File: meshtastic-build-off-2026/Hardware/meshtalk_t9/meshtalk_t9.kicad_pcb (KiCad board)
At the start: 4 copper layers, 45.8 x 79.2 mm, 44 parts, among them J1 USB_C_Receptacle_USB2.0_16P, J2 Conn_01x02_Socket, Q1 Q_PMOS_GSD, SW1 SW_Push, SW10 SW_Push, SW11 SW_Push, SW12 SW_Push, SW13 SW_Push, SW14 SW_Push, SW15 SW_Push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

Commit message: rename + battery % + boot btn changed to reset + fix battery chrging
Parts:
- added Q2: 2N7002, Package_TO_SOT_SMD:SOT-23, F.Cu at (43.8, 66.0)
- added R5: 390k, Capacitor_SMD:C_0805_2012Metric, F.Cu at (46.8, 68.0)
- added R6: 100k, Capacitor_SMD:C_0805_2012Metric, F.Cu at (46.8, 71.8)
- added R7: 2k, Capacitor_SMD:C_0805_2012Metric, F.Cu at (48.8, 46.5)
- moved C6 22.4 mm to (40.0, 63.2)
- moved Q1 2.85 mm to (49.6, 42.2), turned to 180 degrees
- moved SW1 1.75 mm to (54.0, 69.2)
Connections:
- Q1 pad 2: Net-(J2-Pin_1) -> /Power_Management/V_SYS
- Q1 pad 3: /Power_Management/V_SYS -> Net-(J2-Pin_1)
- SW1 pad 2: Net-(U1-IO0) -> Net-(U1-EN)
- U1 pad 15: unconnected-(U1-IO3-Pad15) -> /MCU_Core/BATTERY_PIN
- U1 pad 24: unconnected-(U1-IO47-Pad24) -> /MCU_Core/ADC_CTRL
- U1 pad 27: Net-(U1-IO0) -> unconnected-(U1-IO0-Pad27)
- U3 pad 8: unconnected-(U3-PROG-Pad8) -> Net-(U3-PROG)
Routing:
- net /MCU_Core/BATTERY_PIN: track 0.00 -> 49.3 mm, vias 0 -> 4
- net Net-(U1-EN): track 14.9 -> 60.3 mm, vias 0 -> 2
- net /MCU_Core/ADC_CTRL: track 0.00 -> 19.0 mm
- net Net-(U1-IO0): track 16.2 -> 0.00 mm
- net Net-(J2-Pin_1): track 32.6 -> 40.2 mm
- net Net-(Q2-D): track 0.00 -> 7.16 mm
- net Net-(U3-PROG): track 0.00 -> 2.75 mm
- net GND: track 40.8 -> 42.9 mm, vias 12 -> 14
- net +3V3: track 91.3 -> 93.0 mm, vias 6 -> 5
- net Net-(D1-A): track 33.8 -> 32.4 mm
- net /Power_Management/V_SYS: track 41.2 -> 40.0 mm

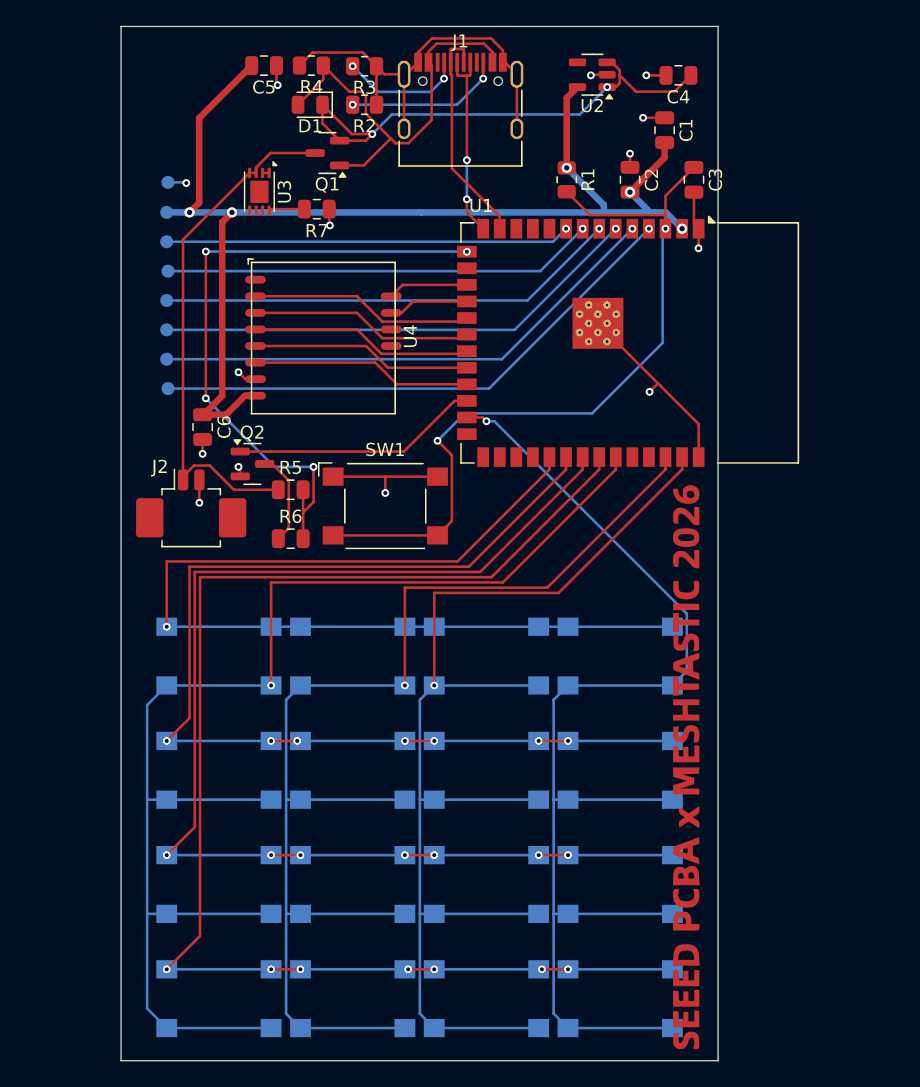
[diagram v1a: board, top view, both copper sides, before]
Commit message: Replace AP2112K-3.3  with AP7361C-33E Connected LORA RF_SW1 to GPIO Added ESD Added mounting holes for display (Waveshare 2 inch) Added Boot and Reset buttons made power rails thicker added dedicated layer for 3v3 and GND
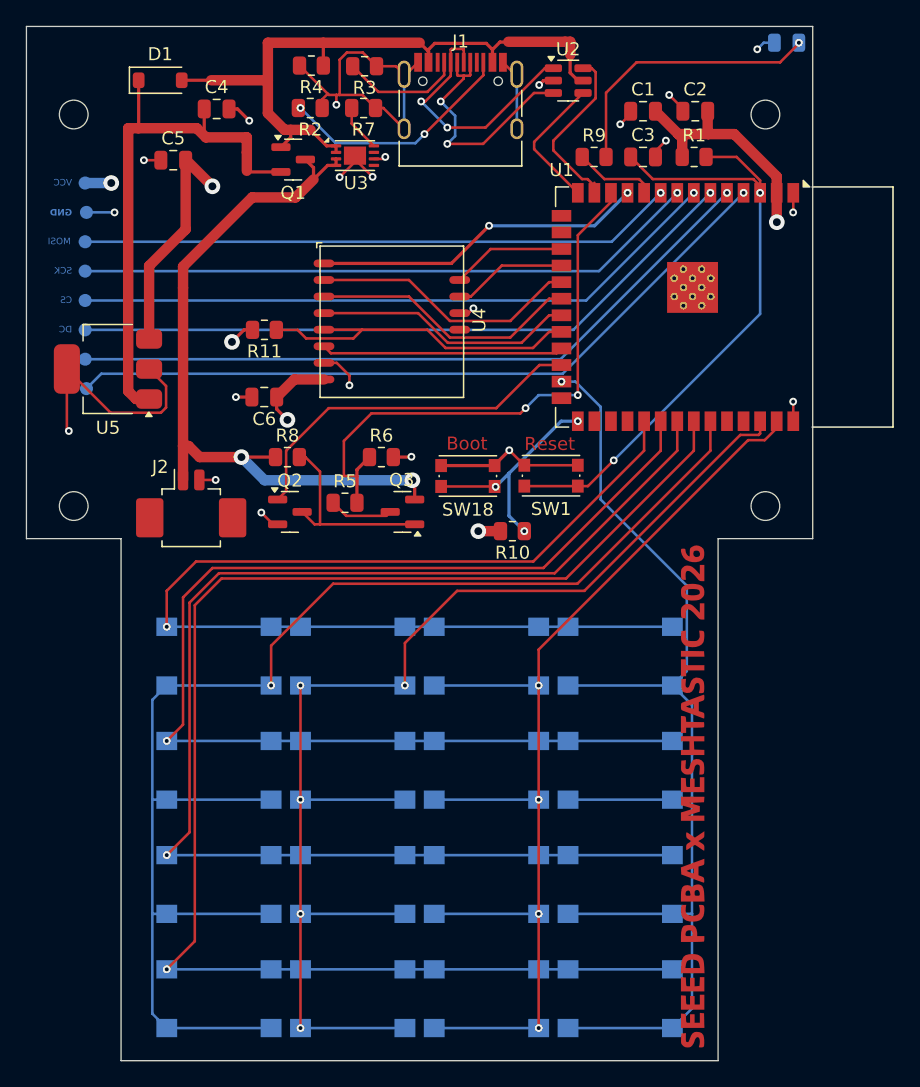
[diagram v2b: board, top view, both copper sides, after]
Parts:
- added D2: LED, LED_SMD:LED_0805_2012Metric, B.Cu at (84.8, 33.8)
- added H1: MountingHole, MountingHole:MountingHole_2.2mm_M2, F.Cu at (83.1, 69.2)
- added H2: MountingHole, MountingHole:MountingHole_2.2mm_M2, F.Cu at (83.1, 39.2)
- added H3: MountingHole, MountingHole:MountingHole_2.2mm_M2, F.Cu at (30.1, 39.2)
- added H4: MountingHole, MountingHole:MountingHole_2.2mm_M2, F.Cu at (30.1, 69.2)
- added Q3: Q_PMOS_GSD, Package_TO_SOT_SMD:SOT-23, F.Cu at (55.3, 69.7)
- added R10: 10k, Resistor_SMD:R_0805_2012Metric, F.Cu at (63.7, 71.2)
- added R11: 10k, Resistor_SMD:R_0805_2012Metric, F.Cu at (44.7, 55.8)
- added R8: 100k, Resistor_SMD:R_0805_2012Metric, F.Cu at (46.5, 65.5)
- added R9: 470, Resistor_SMD:R_0805_2012Metric, F.Cu at (70.0, 42.5)
- added SW18: SW_Push, Button_Switch_SMD:SW_Push_1P1T_NO_CK_KMR2, F.Cu at (60.3, 67.0)
- added U5: AP7361C-33E, Package_TO_SOT_SMD:SOT-223-3_TabPin2, F.Cu at (32.8, 58.8)
- C1, C4, C5: value 10uF -> 10uF 16V X5R
- C3: value 0.1uf -> 0.1uF
- D1: footprint LED_SMD:LED_0805_2012Metric -> Diode_SMD:D_SOD-123
- R5, R6, R7: footprint Capacitor_SMD:C_0805_2012Metric -> Resistor_SMD:R_0805_2012Metric
- SW1: footprint Button_Switch_SMD:SW_SPST_Omron_B3FS-100xP -> Button_Switch_SMD:SW_Push_1P1T_NO_CK_KMR2
- U2: value AP2112K-3.3 -> USBLC6-2SC6; footprint Package_TO_SOT_SMD:SOT-23-5 -> Package_TO_SOT_SMD:SOT-23-6
- moved C4 35.5 mm to (41.1, 38.8), turned to 0 degrees
- moved SW1 12.9 mm to (66.7, 66.9)
- moved D1 11.7 mm to (36.8, 36.6), turned to 0 degrees
- moved C5 10.1 mm to (37.8, 42.8), turned to 0 degrees
- moved R1 9.92 mm to (77.7, 42.5), turned to 0 degrees
- moved R6 9.35 mm to (53.7, 65.5)
- moved R7 8.54 mm to (52.3, 38.8)
- moved U3 7.83 mm to (51.7, 42.4), turned to 0 degrees
- moved U1 7.75 mm to (80.0, 54.0)
- moved TP2 7.70 mm to (31.0, 53.5)
- moved TP4 7.70 mm to (31.0, 58.0)
- moved C2 7.25 mm to (77.8, 39.0), turned to 0 degrees
- moved TP5 6.74 mm to (31.0, 49.0)
- moved TP8 6.66 mm to (31.1, 46.8)
- moved TP6 6.64 mm to (31.0, 51.2)
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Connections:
- net /LoRa_Radio/LORA_DI02 renamed /LoRa_Radio/LORA_BUSY
- J1 pad A1: Net-(J1-SHIELD) -> GND
- J1 pad A12: Net-(J1-SHIELD) -> GND
- J1 pad A6: /MCU_Core/USB_D+ -> Net-(J1-D+-PadA6)
- J1 pad A7: /MCU_Core/USB_D- -> Net-(J1-D--PadA7)
- J1 pad B1: Net-(J1-SHIELD) -> GND
- J1 pad B12: Net-(J1-SHIELD) -> GND
- J1 pad B6: /MCU_Core/USB_D+ -> Net-(J1-D+-PadA6)
- J1 pad B7: /MCU_Core/USB_D- -> Net-(J1-D--PadA7)
- J1 pad S1: Net-(J1-SHIELD) -> GND
- R2 pad 1: Net-(J1-SHIELD) -> GND
- R3 pad 1: Net-(J1-SHIELD) -> GND
- R4 pad 2: Net-(J1-SHIELD) -> GND
- R5 pad 1: Net-(J2-Pin_1) -> Net-(Q3-D)
- R6 pad 1: Net-(Q2-D) -> /MCU_Core/BATTERY_PIN
- R6 pad 2: /MCU_Core/BATTERY_PIN -> GND
- U1 pad 10: unconnected-(U1-IO17-Pad10) -> Net-(U1-IO17)
- U1 pad 11: unconnected-(U1-IO18-Pad11) -> /LoRa_Radio/LORA_RF_SW1
- U1 pad 12: unconnected-(U1-IO8-Pad12) -> /MCU_Core/BATTERY_PIN
- U1 pad 15: /MCU_Core/BATTERY_PIN -> unconnected-(U1-IO3-Pad15)
- U1 pad 27: unconnected-(U1-IO0-Pad27) -> Net-(U1-IO0)
- U1 pad 5: /MCU_Core/DISPLAY_CS -> /MCU_Core/TFT_RST
- U1 pad 7: /MCU_Core/TFT_RST -> /MCU_Core/DISPLAY_CS
- U1 pad 8: /MCU_Core/TFT_MOSI -> /MCU_Core/TFT_SCK
- U1 pad 9: /MCU_Core/TFT_SCK -> /MCU_Core/TFT_MOSI
- U2 pad 1: /Power_Management/V_SYS -> Net-(J1-D--PadA7)
- U2 pad 3: /Power_Management/V_SYS -> Net-(J1-D+-PadA6)
- U2 pad 4: unconnected-(U2-NC-Pad4) -> /MCU_Core/USB_D+
- U2 pad 5: +3V3 -> Net-(D1-A)
- U3 pad 1: Net-(U3-V_{DD}-Pad1) -> Net-(D1-A)
- U3 pad 2: Net-(U3-V_{DD}-Pad1) -> Net-(D1-A)
- U3 pad 6: unconnected-(U3-V_{SS}-Pad6) -> GND
- U3 pad 9: (no net) -> GND
- U4 pad 1: unconnected-(U4-RF_SW1-Pad1) -> /LoRa_Radio/LORA_RF_SW1
- U4 pad 10: unconnected-(U4-GND2-Pad10) -> GND
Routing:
- net GND: track 42.9 -> 91.6 mm, vias 14 -> 22
- net +3V3: track 93.0 -> 48.6 mm, vias 5 -> 6
- net Net-(J1-SHIELD): track 32.3 -> 0.00 mm
- net /LoRa_Radio/LORA_RF_SW1: track 0.00 -> 25.5 mm, vias 0 -> 2
- net Net-(D2-A): track 0.00 -> 21.4 mm, vias 0 -> 1
- net Net-(D1-A): track 32.4 -> 52.6 mm
- net Net-(J1-D--PadA7): track 0.00 -> 19.9 mm, vias 0 -> 2
- net Net-(J1-D+-PadA6): track 0.00 -> 19.4 mm, vias 0 -> 2
- net /MCU_Core/TFT_RST: track 35.4 -> 54.5 mm
- net Net-(U1-IO0): track 0.00 -> 17.5 mm, vias 0 -> 3
- net /MCU_Core/TFT_SCK: track 31.0 -> 47.9 mm
- net Net-(J2-Pin_1): track 40.2 -> 56.5 mm, vias 0 -> 2
- net /MCU_Core/TFT_DC: track 37.6 -> 52.3 mm
- net /MCU_Core/TFT_BL: track 41.9 -> 56.6 mm
- net /MCU_Core/TFT_MOSI: track 33.1 -> 45.7 mm
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- added copper zone on In2.Cu, net +3V3
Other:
- board size 45.8 x 79.2 mm -> 60.2 x 79.2 mm
- board text added: "BL"
- board text added: "Boot"
- board text added: "CS"
- board text added: "DC"
- board text added: "GND"
- board text added: "MOSI"
- board text added: "RST"
- board text added: "Reset"
- board text added: "SCK"
- board text added: "VCC"

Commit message: PCB Updates - Align net names Clearence for esp32 antenna
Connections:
- net /MCU_Core/DISPLAY_CS renamed /MCU_Core/TFT_CS
- net /MCU_Core/TFT_SCK renamed /MCU_Core/TFT_CLK
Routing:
- net GND: track 91.6 -> 129.0 mm, vias 22 -> 21
- net +3V3: track 48.6 -> 70.8 mm
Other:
- board text added: "CLK"
- board text removed: "SCK"
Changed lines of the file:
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@@
 	(net 34 "/MCU_Core/TFT_RST")
 	(net 35 "Net-(Q2-D)")
-	(net 36 "/MCU_Core/DISPLAY_CS")
+	(net 36 "/MCU_Core/TFT_CS")
 	(net 37 "/MCU_Core/TFT_BL")
 	(net 38 "unconnected-(U3-STAT-Pad5)")
@@
 	(net 40 "unconnected-(U4-ANT-Pad9)")
 	(net 41 "/MCU_Core/TFT_MOSI")
-	(net 42 "/MCU_Core/TFT_SCK")
+	(net 42 "/MCU_Core/TFT_CLK")
 	(net 43 "/LoRa_Radio/SPI_MOSI_LORA")
 	(net 44 "/LoRa_Radio/SPI_MISO_LORA")
@@
 			)
 		)
-		(property "MPN" "ESP32-S3-WROOM-1-N16R16VA"
+		(property "MPN" "ESP32-S3-WROOM-1-N16R8"
 			(at 0 0 270)
 			(unlocked yes)
@@
 			(size 1.5 0.9)
 			(layers "F.Cu" "F.Mask" "F.Paste")
-			(net 36 "/MCU_Core/DISPLAY_CS")
+			(net 36 "/MCU_Core/TFT_CS")
 			(pinfunction "IO7")
 			(pintype "bidirectional")
@@
 			(size 1.5 0.9)
 			(layers "F.Cu" "F.Mask" "F.Paste")
-			(net 42 "/MCU_Core/TFT_SCK")
+			(net 42 "/MCU_Core/TFT_CLK")
 			(pinfunction "IO15")
 			(pintype "bidirectional")
@@
 			(size 1 1)
 			(layers "B.Cu" "B.Mask")
-			(net 36 "/MCU_Core/DISPLAY_CS")
+			(net 36 "/MCU_Core/TFT_CS")
 			(pinfunction "1")
 			(pintype "passive")
@@
 			(size 1 1)
 			(layers "B.Cu" "B.Mask")
-			(net 42 "/MCU_Core/TFT_SCK")
+			(net 42 "/MCU_Core/TFT_CLK")
 			(pinfunction "1")
 			(pintype "passive")
@@
 		)
 	)
-	(gr_text "SCK"
+	(gr_text "CLK"
 		(at 30 51.5 0)
 		(layer "B.Cu")
@@
 	)
 	(segment
+		(start 83.99 45.25)
+		(end 83.99 55.81)
+		(width 0.8)
+		(layer "F.Cu")
+		(net 1)
+	)
+	(segment
 		(start 38.75 42.75)
 		(end 40.75 44.75)
@@
 	)
 	(segment
-		(start 83.99 47.49)
-		(end 84 47.5)
-		(width 0.8)
-		(layer "F.Cu")
-		(net 1)
-	)
-	(segment
 		(start 45.675 61.825)
 		(end 46.5 62.65)
@@
 	)
 	(segment
-		(start 78.7 39)
-		(end 78.7 40.7)
+		(start 83.99 55.81)
+		(end 81.425 58.375)
 		(width 0.8)
 		(layer "F.Cu")
@@
 	)
 	(segment
-		(start 83.99 45.25)
-		(end 83.99 47.49)
+		(start 78.7 39)
+		(end 78.7 40.7)
 		(width 0.8)
 		(layer "F.Cu")
@@
 	)
 	(segment
+		(start 81.425 58.375)
+		(end 81.075 58.725)
+		(width 0.8)
+		(layer "F.Cu")
+		(net 1)
+	)
+	(segment
 		(start 83.99 44)
 		(end 80.74 40.75)
@@
 	)
 	(segment
+		(start 81.075 58.725)
+		(end 71.325 58.725)
+		(width 0.8)
+		(layer "F.Cu")
+		(net 1)
+	)
+	(segment
 		(start 83.99 44)
 		(end 83.99 45.25)
@@
 	)
 	(via
-		(at 84 47.5)
+		(at 33 44.5)
 		(size 1.2)
 		(drill 0.6)
@@
 	)
 	(via
-		(at 33 44.5)
+		(at 40.75 44.75)
 		(size 1.2)
 		(drill 0.6)
@@
 	)
 	(via
-		(at 40.75 44.75)
+		(at 42.25 56.675)
 		(size 1.2)
 		(drill 0.6)
@@
 	)
 	(via
-		(at 42.25 56.675)
+		(at 71.325 58.725)
 		(size 1.2)
 		(drill 0.6)
@@
 	)
 	(segment
-		(start 74.7 42.05)
-		(end 75.5 41.25)
+		(start 84.01 60.55)
+		(end 71.2 60.55)
 		(width 0.2)
 		(layer "F.Cu")
@@
 	)
 	(segment
-		(start 85.26 46.74)
-		(end 85.25 46.75)
+		(start 74.7 42.05)
+		(end 75.5 41.25)
 		(width 0.2)
 		(layer "F.Cu")
@@
 	)
 	(segment
+		(start 85.26 62.75)
+		(end 85.26 61.8)
+		(width 0.2)
+		(layer "F.Cu")
+		(net 2)
+	)
+	(segment
 		(start 51.675 42.4)
 		(end 51.675 42.875)
@@
 	)
 	(segment
+		(start 85.26 45.25)
+		(end 85.26 59.3)
+		(width 0.2)
+		(layer "F.Cu")
+		(net 2)
+	)
+	(segment
 		(start 66.875 36.65)
 		(end 66.126314 36.65)
@@
 	)
 	(segment
-		(start 85.26 61.26)
-		(end 85.25 61.25)
-		(width 0.2)
-		(layer "F.Cu")
-		(net 2)
-	)
-	(segment
 		(start 49.674 37.749)
 		(end 50.25 37.749)
@@
 	)
 	(segment
-		(start 85.26 62.75)
-		(end 85.26 61.26)
-		(width 0.2)
-		(layer "F.Cu")
-		(net 2)
-	)
-	(segment
 		(start 51.25 59.25)
 		(end 51.25 60)
@@
 	)
 	(segment
+		(start 85.26 61.8)
+		(end 84.01 60.55)
+		(width 0.2)
+		(layer "F.Cu")
+		(net 2)
+	)
+	(segment
 		(start 76.8 38.8)
 		(end 75.75 37.75)
@@
 	)
 	(segment
-		(start 85.26 45.25)
-		(end 85.26 46.74)
-		(width 0.2)
-		(layer "F.Cu")
-		(net 2)
-	)
-	(segment
 		(start 42.675 38.825)
 		(end 43.575 39.725)
@@
 	)
 	(segment
+		(start 85.26 59.3)
+		(end 84.01 60.55)
+		(width 0.2)
+		(layer "F.Cu")
+		(net 2)
+	)
+	(segment
 		(start 62.375 66.15)
 		(end 62.375 66.1)
@@
 	)
 	(via
-		(at 85.25 61.25)
-		(size 0.6)
-		(drill 0.3)
-		(layers "F.Cu" "B.Cu")
-		(net 2)
-	)
-	(via
 		(at 56 65.475)
 		(size 0.6)
@@
 	)
 	(via
-		(at 82.5 34.25)
+		(at 33.25 46.75)
 		(size 0.6)
 		(drill 0.3)
@@
 	)
 	(via
-		(at 33.25 46.75)
+		(at 35.5 42.75)
 		(size 0.6)
 		(drill 0.3)
@@
 	)
 	(via
-		(at 35.5 42.75)
+		(at 65.788157 36.988157)
 		(size 0.6)
 		(drill 0.3)
@@
 	)
 	(via
-		(at 65.788157 36.988157)
+		(at 73.225 33.75)
 		(size 0.6)
 		(drill 0.3)
@@
 	)
 	(via
-		(at 85.25 46.75)
+		(at 71.2 60.55)
 		(size 0.6)
 		(drill 0.3)
@@
 	)
 	(segment
-		(start 83 33.75)
-		(end 82.5 34.25)
-		(width 0.2)
-		(layer "B.Cu")
-		(net 2)
-	)
-	(segment
 		(start 83.8125 33.75)
-		(end 83 33.75)
+		(end 73.225 33.75)
 		(width 0.2)
 		(layer "B.Cu")
@@
 		(polygon
 			(pts
-				(xy 27.5 32.75) (xy 27.5 111.75) (xy 86.75 111.75) (xy 86.75 32.75)
+				(xy 27.5 32.75) (xy 27.5 111.75) (xy 79.5 111.75) (xy 79.5 32.75)
 			)
 		)
@@
 			(pts
 				(xy 26.5 32.5) (xy 26.5 71.75) (xy 33.75 71.75) (xy 33.75 111.75) (xy 79.5 111.75) (xy 79.5 71.75)
-				(xy 86.75 71.75) (xy 86.75 32.5)
+				(xy 79.5 71.75) (xy 79.5 32.5)
 			)
 		)
